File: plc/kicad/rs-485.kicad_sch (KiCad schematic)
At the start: 10 parts, among them CN12 DB2ERC-5.08-4P, SW5 MSK12C02, U19 THVD1450DR

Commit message: Added more wiring
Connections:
- net EXT_RS485_A: now also CN12.4, D16.2; no longer CN12.3, D16.1
- net EXT_RS485_B: now also CN12.3, D16.1; no longer CN12.4, D16.2
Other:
- moved on the sheet: D16
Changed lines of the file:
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@@
 	)
 	(junction
-		(at 70.485 73.66)
+		(at 69.85 71.12)
 		(diameter 0)
 		(color 0 0 0 0)
 	)
 	(junction
-		(at 65.405 71.12)
+		(at 64.77 73.66)
 		(diameter 0)
 		(color 0 0 0 0)
@@
 	(wire
 		(pts
-			(xy 47.625 73.66) (xy 70.485 73.66)
-		)
-		(stroke
-			(width 0)
-			(type default)
-		)
-	)
-	(wire
-		(pts
-			(xy 65.405 71.12) (xy 78.74 71.12)
+			(xy 47.625 73.66) (xy 64.77 73.66)
 		)
 		(stroke
@@
 	(wire
 		(pts
-			(xy 65.405 71.12) (xy 65.405 79.375)
-		)
-		(stroke
-			(width 0)
-			(type default)
-		)
-	)
-	(wire
-		(pts
 			(xy 201.93 126.365) (xy 201.93 127.635)
 		)
@@
 	(wire
 		(pts
+			(xy 64.77 73.66) (xy 64.77 79.375)
+		)
+		(stroke
+			(width 0)
+			(type default)
+		)
+	)
+	(wire
+		(pts
 			(xy 86.36 79.375) (xy 86.36 76.2)
 		)
@@
 	(wire
 		(pts
-			(xy 67.945 95.885) (xy 67.945 94.615)
+			(xy 67.31 94.615) (xy 67.31 95.885)
+		)
+		(stroke
+			(width 0)
+			(type default)
+		)
+	)
+	(wire
+		(pts
+			(xy 69.85 79.375) (xy 69.85 71.12)
 		)
 		(stroke
@@
 	(wire
 		(pts
-			(xy 47.625 71.12) (xy 65.405 71.12)
+			(xy 47.625 71.12) (xy 69.85 71.12)
 		)
 		(stroke
@@
 	(wire
 		(pts
-			(xy 70.485 73.66) (xy 70.485 79.375)
-		)
-		(stroke
-			(width 0)
-			(type default)
-		)
-	)
-	(wire
-		(pts
 			(xy 191.77 136.525) (xy 191.77 138.43)
 		)
@@
 	(wire
 		(pts
+			(xy 64.77 73.66) (xy 70.485 73.66)
+		)
+		(stroke
+			(width 0)
+			(type default)
+		)
+	)
+	(wire
+		(pts
 			(xy 201.93 127.635) (xy 191.77 127.635)
 		)
@@
 		(pts
 			(xy 68.58 124.46) (xy 82.55 124.46)
+		)
+		(stroke
+			(width 0)
+			(type default)
+		)
+	)
+	(wire
+		(pts
+			(xy 69.85 71.12) (xy 78.74 71.12)
 		)
 		(stroke
@@
 		)
 	)
-	(label "EXT_RS485_B"
-		(at 188.595 106.68 0)
-		(effects
-			(font
-				(size 1.27 1.27)
-			)
-			(justify left bottom)
-		)
-	)
 	(label "RS485_RXD"
 		(at 120.65 68.58 180)
@@
 	)
 	(label "EXT_RS485_B"
+		(at 188.595 104.14 0)
+		(effects
+			(font
+				(size 1.27 1.27)
+			)
+			(justify left bottom)
+		)
+	)
+	(label "EXT_RS485_B"
 		(at 82.55 124.46 180)
 		(effects
@@
 	)
 	(label "EXT_RS485_A"
+		(at 188.595 106.68 0)
+		(effects
+			(font
+				(size 1.27 1.27)
+			)
+			(justify left bottom)
+		)
+	)
+	(label "EXT_RS485_A"
 		(at 47.625 73.66 0)
 		(effects
@@
 	(label "RS485_DIR"
 		(at 177.165 147.955 0)
-		(effects
-			(font
-				(size 1.27 1.27)
-			)
-			(justify left bottom)
-		)
-	)
-	(label "EXT_RS485_A"
-		(at 188.595 104.14 0)
 		(effects
 			(font
@@
 	(symbol
 		(lib_id "LibrePLC32:CDSOT23-SM712")
-		(at 67.945 86.995 180)
+		(at 67.31 86.995 180)
 		(unit 1)
 		(body_style 1)
@@
 		(dnp no)
 		(property "Reference" "D16"
-			(at 69.85 92.71 0)
+			(at 69.215 92.71 0)
 			(show_name no)
 			(do_not_autoplace no)
@@
 		)
 		(property "Value" "CDSOT23-SM712"
-			(at 69.85 95.25 0)
+			(at 69.215 95.25 0)
 			(show_name no)
 			(do_not_autoplace no)
@@
 		)
 		(property "Footprint" "LibrePLC32:SOT-23_L2.9-W1.3-P1.90-LS2.4-BR"
-			(at 67.945 71.755 0)
+			(at 67.31 71.755 0)
 			(hide yes)
 			(show_name no)
@@
 		)
 		(property "Datasheet" "https://lcsc.com/product-detail/Diodes-ESD_BOURNS-CDSOT23-SM712_C404012.html"
-			(at 67.945 69.215 0)
+			(at 67.31 69.215 0)
 			(hide yes)
 			(show_name no)
@@
 		)
 		(property "Description" ""
-			(at 67.945 86.995 0)
+			(at 67.31 86.995 0)
 			(hide yes)
 			(show_name no)
@@
 		)
 		(property "Manufacturer" "BOURNS"
-			(at 67.945 66.675 0)
+			(at 67.31 66.675 0)
 			(hide yes)
 			(show_name no)
@@
 		)
 		(property "MPN" "CDSOT23-SM712"
-			(at 67.945 64.135 0)
+			(at 67.31 64.135 0)
 			(hide yes)
 			(show_name no)
@@
 		)
 		(property "LCSC Part" "C404012"
-			(at 67.945 61.595 0)
+			(at 67.31 61.595 0)
 			(hide yes)
 			(show_name no)
@@
 	(symbol
 		(lib_id "power:GND")
-		(at 67.945 95.885 0)
+		(at 67.31 95.885 0)
 		(unit 1)
 		(body_style 1)
@@
 		(fields_autoplaced yes)
 		(property "Reference" "#PWR0202"
-			(at 67.945 102.235 0)
+			(at 67.31 102.235 0)
 			(hide yes)
 			(show_name no)
@@
 		)
 		(property "Value" "GND"
-			(at 67.945 100.203 0)
+			(at 67.31 100.203 0)
 			(show_name no)
 			(do_not_autoplace no)
@@
 		)
 		(property "Footprint" ""
-			(at 67.945 95.885 0)
+			(at 67.31 95.885 0)
 			(hide yes)
 			(show_name no)
@@
 		)
 		(property "Datasheet" ""
-			(at 67.945 95.885 0)
+			(at 67.31 95.885 0)
 			(hide yes)
 			(show_name no)
@@
 		)
 		(property "Description" "Power symbol creates a global label with name \"GND\" , ground"
-			(at 67.945 95.885 0)
-			(hide yes)
-			(show_name no)
+			(at 67.31 95.885 0)
+			(hide yes)
+			(show_name no)

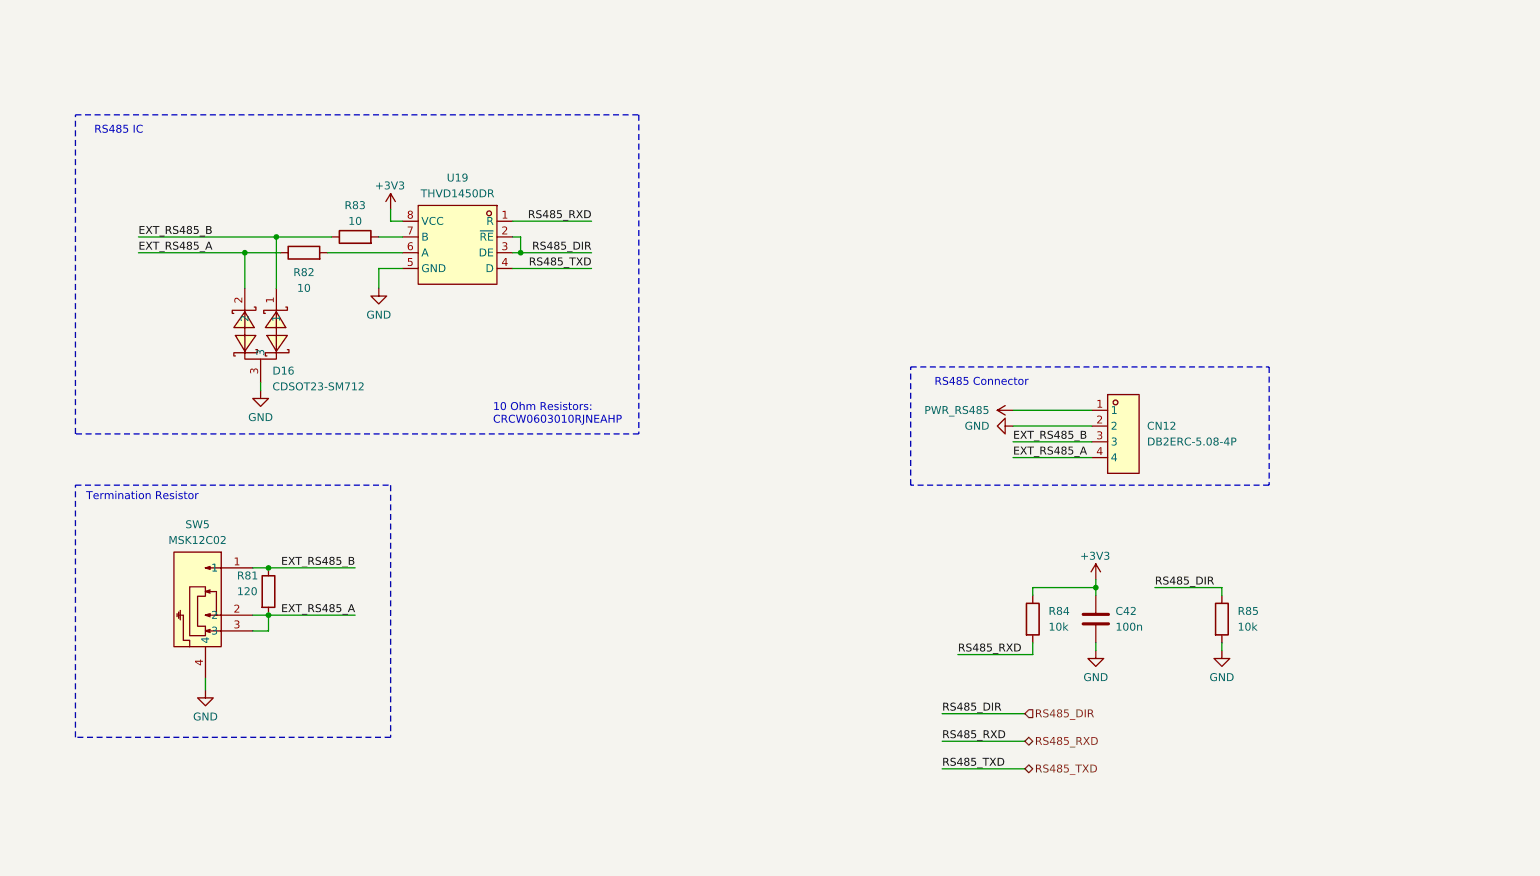
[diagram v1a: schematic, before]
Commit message: Rearranged small PCB placements
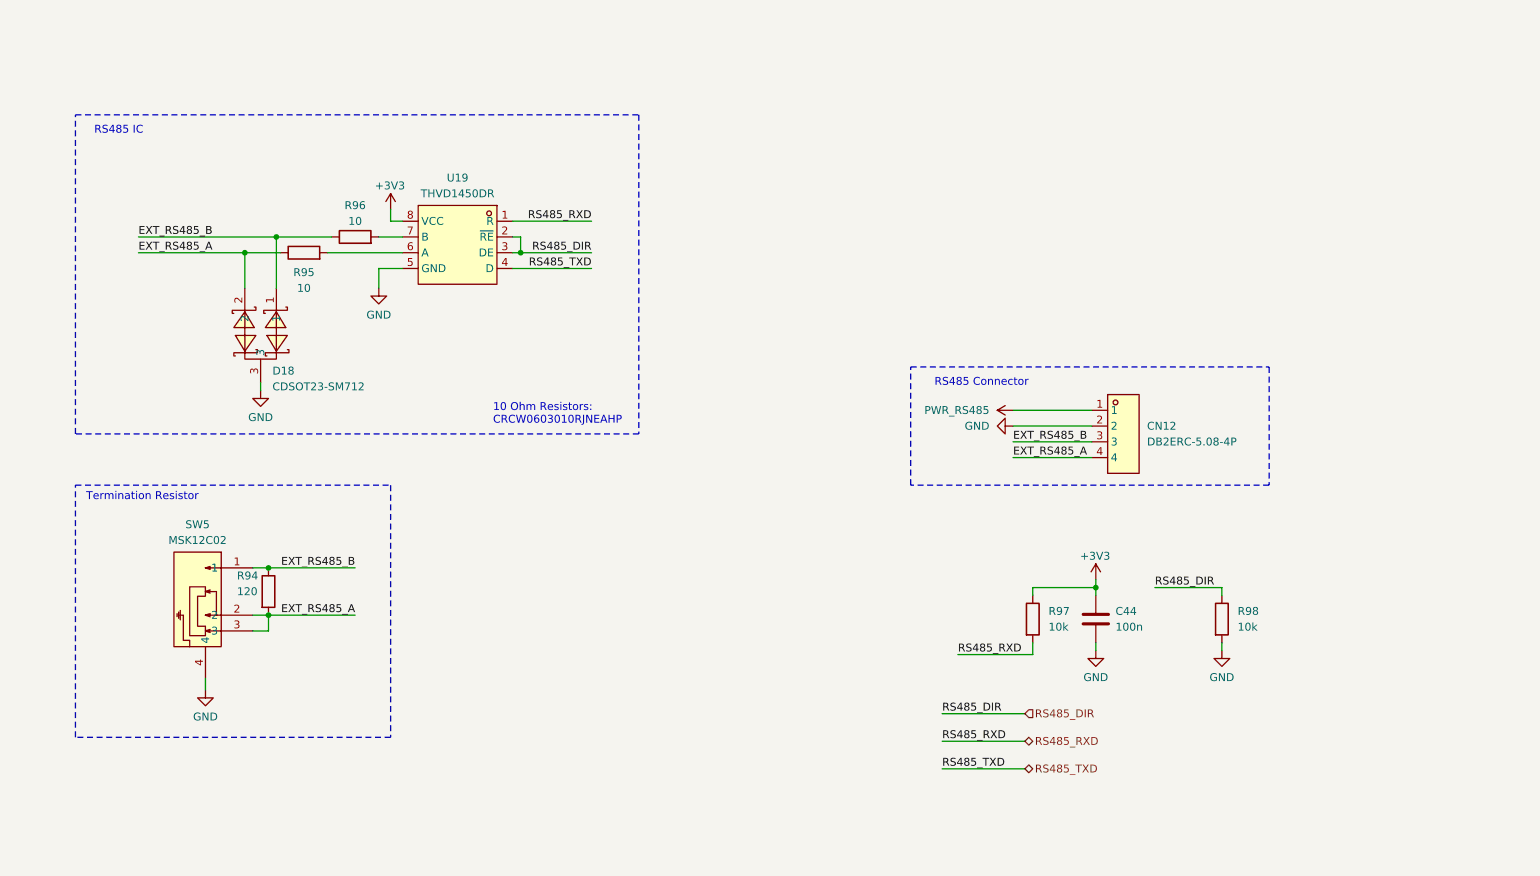
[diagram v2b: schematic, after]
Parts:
- renumbered C42 to C44, D16 to D18, R81 to R94, R82 to R95, R83 to R96, R84 to R97, R85 to R98
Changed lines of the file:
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@@
 		(in_pos_files yes)
 		(dnp no)
-		(property "Reference" "#PWR0246"
+		(property "Reference" "#PWR0217"
 			(at 88.265 70.485 0)
 			(hide yes)
@@
 			(project "LibrePLC32"
 				(path "/ef4c1a27-85a3-413a-9f93-a41c4f97eee5/58fa1ecb-ea1c-4a70-bb90-31ff9b441562"
-					(reference "#PWR0246")
+					(reference "#PWR0217")
 					(unit 1)
 				)
@@
 		(dnp no)
 		(fields_autoplaced yes)
-		(property "Reference" "#PWR0208"
+		(property "Reference" "#PWR0222"
 			(at 222.25 144.145 0)
 			(hide yes)
@@
 			(project "LibrePLC32"
 				(path "/ef4c1a27-85a3-413a-9f93-a41c4f97eee5/58fa1ecb-ea1c-4a70-bb90-31ff9b441562"
-					(reference "#PWR0208")
+					(reference "#PWR0222")
 					(unit 1)
 				)
@@
 		(dnp no)
 		(fields_autoplaced yes)
-		(property "Reference" "#PWR0203"
+		(property "Reference" "#PWR0216"
 			(at 86.36 85.725 0)
 			(hide yes)
@@
 			(project "LibrePLC32"
 				(path "/ef4c1a27-85a3-413a-9f93-a41c4f97eee5/58fa1ecb-ea1c-4a70-bb90-31ff9b441562"
-					(reference "#PWR0203")
+					(reference "#PWR0216")
 					(unit 1)
 				)
@@
 		(dnp no)
 		(fields_autoplaced yes)
-		(property "Reference" "R85"
+		(property "Reference" "R98"
 			(at 224.79 131.4449 0)
 			(show_name no)
@@
 			(project "LibrePLC32"
 				(path "/ef4c1a27-85a3-413a-9f93-a41c4f97eee5/58fa1ecb-ea1c-4a70-bb90-31ff9b441562"
-					(reference "R85")
+					(reference "R98")
 					(unit 1)
 				)
@@
 		(in_pos_files yes)
 		(dnp no)
-		(property "Reference" "D16"
+		(property "Reference" "D18"
 			(at 69.215 92.71 0)
 			(show_name no)
@@
 			(project "LibrePLC32"
 				(path "/ef4c1a27-85a3-413a-9f93-a41c4f97eee5/58fa1ecb-ea1c-4a70-bb90-31ff9b441562"
-					(reference "D16")
+					(reference "D18")
 					(unit 1)
 				)
@@
 		(in_pos_files yes)
 		(dnp no)
-		(property "Reference" "R81"
+		(property "Reference" "R94"
 			(at 63.5 125.73 0)
 			(show_name no)
@@
 			(project "LibrePLC32"
 				(path "/ef4c1a27-85a3-413a-9f93-a41c4f97eee5/58fa1ecb-ea1c-4a70-bb90-31ff9b441562"
-					(reference "R81")
+					(reference "R94")
 					(unit 1)
 				)
@@
 		(in_pos_files yes)
 		(dnp no)
-		(property "Reference" "#PWR0206"
+		(property "Reference" "#PWR0220"
 			(at 201.93 130.175 0)
 			(hide yes)
@@
 			(project "LibrePLC32"
 				(path "/ef4c1a27-85a3-413a-9f93-a41c4f97eee5/58fa1ecb-ea1c-4a70-bb90-31ff9b441562"
-					(reference "#PWR0206")
+					(reference "#PWR0220")
 					(unit 1)
 				)
@@
 		(in_pos_files yes)
 		(dnp no)
-		(property "Reference" "R83"
+		(property "Reference" "R96"
 			(at 82.55 66.04 90)
 			(show_name no)
@@
 			(project "LibrePLC32"
 				(path "/ef4c1a27-85a3-413a-9f93-a41c4f97eee5/58fa1ecb-ea1c-4a70-bb90-31ff9b441562"
-					(reference "R83")
+					(reference "R96")
 					(unit 1)
 				)
@@
 		(dnp no)
 		(fields_autoplaced yes)
-		(property "Reference" "#PWR0204"
+		(property "Reference" "#PWR0218"
 			(at 192.405 99.06 0)
 			(hide yes)
@@
 			(project "LibrePLC32"
 				(path "/ef4c1a27-85a3-413a-9f93-a41c4f97eee5/58fa1ecb-ea1c-4a70-bb90-31ff9b441562"
-					(reference "#PWR0204")
+					(reference "#PWR0218")
 					(unit 1)
 				)
@@
 		(dnp no)
 		(fields_autoplaced yes)
-		(property "Reference" "C42"
+		(property "Reference" "C44"
 			(at 205.105 131.4449 0)
 			(show_name no)
@@
 			(project "LibrePLC32"
 				(path "/ef4c1a27-85a3-413a-9f93-a41c4f97eee5/58fa1ecb-ea1c-4a70-bb90-31ff9b441562"
-					(reference "C42")
+					(reference "C44")
 					(unit 1)
 				)
@@
 		(dnp no)
 		(fields_autoplaced yes)
-		(property "Reference" "#PWR0202"
+		(property "Reference" "#PWR0215"
 			(at 67.31 102.235 0)
 			(hide yes)
@@
 			(project "LibrePLC32"
 				(path "/ef4c1a27-85a3-413a-9f93-a41c4f97eee5/58fa1ecb-ea1c-4a70-bb90-31ff9b441562"
-					(reference "#PWR0202")
+					(reference "#PWR0215")
 					(unit 1)
 				)
@@
 		(in_pos_files yes)
 		(dnp no)
-		(property "Reference" "R82"
+		(property "Reference" "R95"
 			(at 74.295 76.835 90)
 			(show_name no)
@@
 			(project "LibrePLC32"
 				(path "/ef4c1a27-85a3-413a-9f93-a41c4f97eee5/58fa1ecb-ea1c-4a70-bb90-31ff9b441562"
-					(reference "R82")
+					(reference "R95")
 					(unit 1)
 				)
@@
 		(dnp no)
 		(fields_autoplaced yes)
-		(property "Reference" "#PWR0201"
+		(property "Reference" "#PWR0214"
 			(at 58.42 150.495 0)
 			(hide yes)
@@
 			(project "LibrePLC32"
 				(path "/ef4c1a27-85a3-413a-9f93-a41c4f97eee5/58fa1ecb-ea1c-4a70-bb90-31ff9b441562"
-					(reference "#PWR0201")
+					(reference "#PWR0214")
 					(unit 1)
 				)
@@
 		(dnp no)
 		(fields_autoplaced yes)
-		(property "Reference" "R84"
+		(property "Reference" "R97"
 			(at 194.31 131.4449 0)
 			(show_name no)
@@
 			(project "LibrePLC32"
 				(path "/ef4c1a27-85a3-413a-9f93-a41c4f97eee5/58fa1ecb-ea1c-4a70-bb90-31ff9b441562"
-					(reference "R84")
+					(reference "R97")
 					(unit 1)
 				)
@@
 		(dnp no)
 		(fields_autoplaced yes)
-		(property "Reference" "#PWR0205"
+		(property "Reference" "#PWR0219"
 			(at 182.245 101.6 0)
 			(hide yes)
@@
 			(project "LibrePLC32"
 				(path "/ef4c1a27-85a3-413a-9f93-a41c4f97eee5/58fa1ecb-ea1c-4a70-bb90-31ff9b441562"
-					(reference "#PWR0205")
+					(reference "#PWR0219")
 					(unit 1)
 				)
@@
 		(dnp no)
 		(fields_autoplaced yes)
-		(property "Reference" "#PWR0207"
+		(property "Reference" "#PWR0221"
 			(at 201.93 144.145 0)
 			(hide yes)
@@
 			(project "LibrePLC32"
 				(path "/ef4c1a27-85a3-413a-9f93-a41c4f97eee5/58fa1ecb-ea1c-4a70-bb90-31ff9b441562"
-					(reference "#PWR0207")
-					(unit 1)
-				)
+					(reference "#PWR0221")
+					(unit 1)
+				)

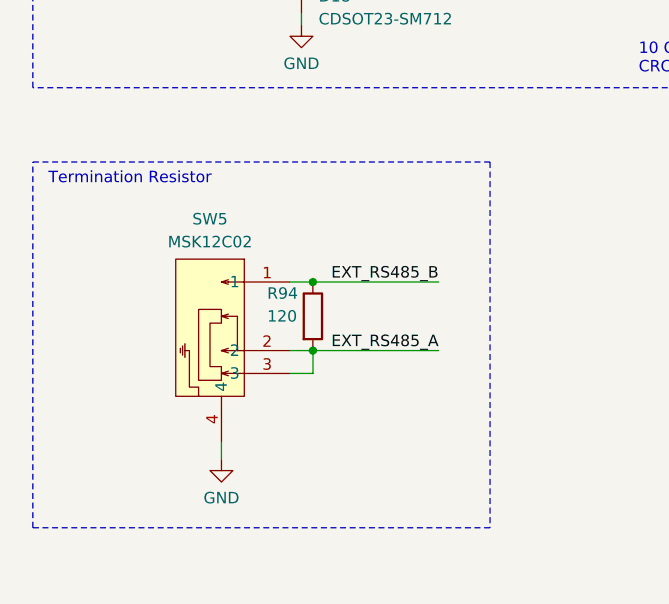
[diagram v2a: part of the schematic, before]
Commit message: Fixed shorting resistors for CAN & RS485
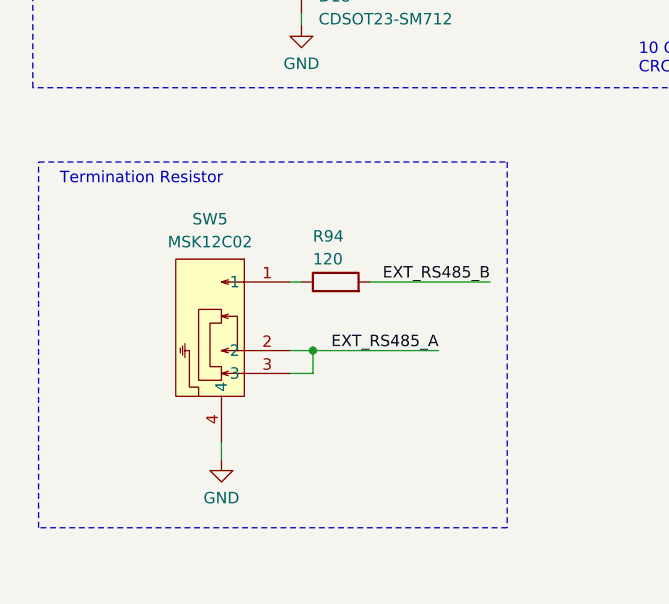
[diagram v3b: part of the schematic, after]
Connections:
- net EXT_RS485_A: no longer R94.2
- net EXT_RS485_B: now also R94.2; no longer R94.1, SW5.1
- new net: R94.1, SW5.1
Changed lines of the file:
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@@
 	)
 	(rectangle
-		(start 37.465 111.125)
-		(end 88.265 151.765)
+		(start 38.1 111.125)
+		(end 90.17 151.765)
 		(stroke
 			(width 0)
@@
 	(text "Termination Resistor"
 		(exclude_from_sim no)
-		(at 48.26 113.03 0)
+		(at 49.53 113.03 0)
 		(effects
 			(font
@@
 	)
 	(junction
-		(at 68.58 124.46)
-		(diameter 0)
-		(color 0 0 0 0)
-	)
-	(junction
 		(at 201.93 127.635)
 		(diameter 0)
@@
 	(wire
 		(pts
-			(xy 66.04 124.46) (xy 68.58 124.46)
+			(xy 74.93 124.46) (xy 88.265 124.46)
 		)
 		(stroke
@@
 	(wire
 		(pts
+			(xy 67.31 124.46) (xy 66.04 124.46)
+		)
+		(stroke
+			(width 0)
+			(type default)
+		)
+	)
+	(wire
+		(pts
 			(xy 191.77 136.525) (xy 191.77 138.43)
 		)
@@
 		(pts
 			(xy 109.22 73.66) (xy 120.65 73.66)
-		)
-		(stroke
-			(width 0)
-			(type default)
-		)
-	)
-	(wire
-		(pts
-			(xy 68.58 124.46) (xy 82.55 124.46)
 		)
 		(stroke
@@
 	)
 	(label "EXT_RS485_B"
-		(at 82.55 124.46 180)
+		(at 88.265 124.46 180)
 		(effects
 			(font
@@
 	)
 	(symbol
-		(lib_id "Device:R")
-		(at 68.58 128.27 0)
-		(unit 1)
-		(body_style 1)
-		(exclude_from_sim no)
-		(in_bom yes)
-		(on_board yes)
-		(in_pos_files yes)
-		(dnp no)
-		(property "Reference" "R94"
-			(at 63.5 125.73 0)
-			(show_name no)
-			(do_not_autoplace no)
-			(effects
-				(font
-					(size 1.27 1.27)
-				)
-				(justify left)
-			)
-		)
-		(property "Value" "120"
-			(at 63.5 128.27 0)
-			(show_name no)
-			(do_not_autoplace no)
-			(effects
-				(font
-					(size 1.27 1.27)
-				)
-				(justify left)
-			)
-		)
-		(property "Footprint" "Resistor_SMD:R_0603_1608Metric"
-			(at 66.802 128.27 90)
-			(hide yes)
-			(show_name no)
-			(do_not_autoplace no)
-			(effects
-				(font
-					(size 1.27 1.27)
-				)
-			)
-		)
-		(property "Datasheet" ""
-			(at 68.58 128.27 0)
-			(hide yes)
-			(show_name no)
-			(do_not_autoplace no)
-			(effects
-				(font
-					(size 1.27 1.27)
-				)
-			)
-		)
-		(property "Description" "Resistor"
-			(at 68.58 128.27 0)
-			(hide yes)
-			(show_name no)
-			(do_not_autoplace no)
-			(effects
-				(font
-					(size 1.27 1.27)
-				)
-			)
-		)
-		(pin "2"
-		)
-		(pin "1"
-		)
-		(instances
-			(project "LibrePLC32"
-				(path "/ef4c1a27-85a3-413a-9f93-a41c4f97eee5/58fa1ecb-ea1c-4a70-bb90-31ff9b441562"
-					(reference "R94")
-					(unit 1)
-				)
-			)
-		)
-	)
-	(symbol
 		(lib_id "LibrePLC32:MSK12C02")
 		(at 59.69 132.08 270)
@@
 					(unit 1)
 				)
+			)
+		)
+	)
+	(symbol
+		(lib_id "Device:R")
+		(at 71.12 124.46 90)
+		(unit 1)
+		(body_style 1)
+		(exclude_from_sim no)
+		(in_bom yes)
+		(on_board yes)
+		(in_pos_files yes)
+		(dnp no)
+		(property "Reference" "R94"
+			(at 68.58 119.38 90)
+			(show_name no)
+			(do_not_autoplace no)
+			(effects
+				(font
+					(size 1.27 1.27)
+				)
+				(justify right)
+			)
+		)
+		(property "Value" "120"
+			(at 68.58 121.92 90)
+			(show_name no)
+			(do_not_autoplace no)
+			(effects
+				(font
+					(size 1.27 1.27)
+				)
+				(justify right)
+			)
+		)
+		(property "Footprint" "Resistor_SMD:R_0603_1608Metric"
+			(at 71.12 126.238 90)
+			(hide yes)
+			(show_name no)
+			(do_not_autoplace no)
+			(effects
+				(font
+					(size 1.27 1.27)
+				)
+			)
+		)
+		(property "Datasheet" ""
+			(at 71.12 124.46 0)
+			(hide yes)
+			(show_name no)
+			(do_not_autoplace no)
+			(effects
+				(font
+					(size 1.27 1.27)
+				)
+			)
+		)
+		(property "Description" "Resistor"
+			(at 71.12 124.46 0)
+			(hide yes)
+			(show_name no)
+			(do_not_autoplace no)
+			(effects
+				(font
+					(size 1.27 1.27)
+				)
+			)
+		)
+		(pin "2"
+		)
+		(pin "1"
+		)
+		(instances
+			(project "LibrePLC32"
+				(path "/ef4c1a27-85a3-413a-9f93-a41c4f97eee5/58fa1ecb-ea1c-4a70-bb90-31ff9b441562"
+					(reference "R94")
+					(unit 1)
+				)
